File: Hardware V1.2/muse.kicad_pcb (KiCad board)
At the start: 2 copper layers, 71.6 x 61.5 mm, 53 parts, among them P1 3.5mm_line, P2 3.5mm_line, P3 RCA, P4 RCA, P8 ATX_PS_ON, P9 LED_Signal, Q1 FQP30N06L, Q2 FQP30N06L, Q3 FQP30N06L, Q4 FQP30N06L, Q5 FQP30N06L, Q6 FQP30N06L, SW1 PWR_SW, U1 MSGEQ7, U2 MSGEQ7, U3 74LS595, U4 Spark_Core

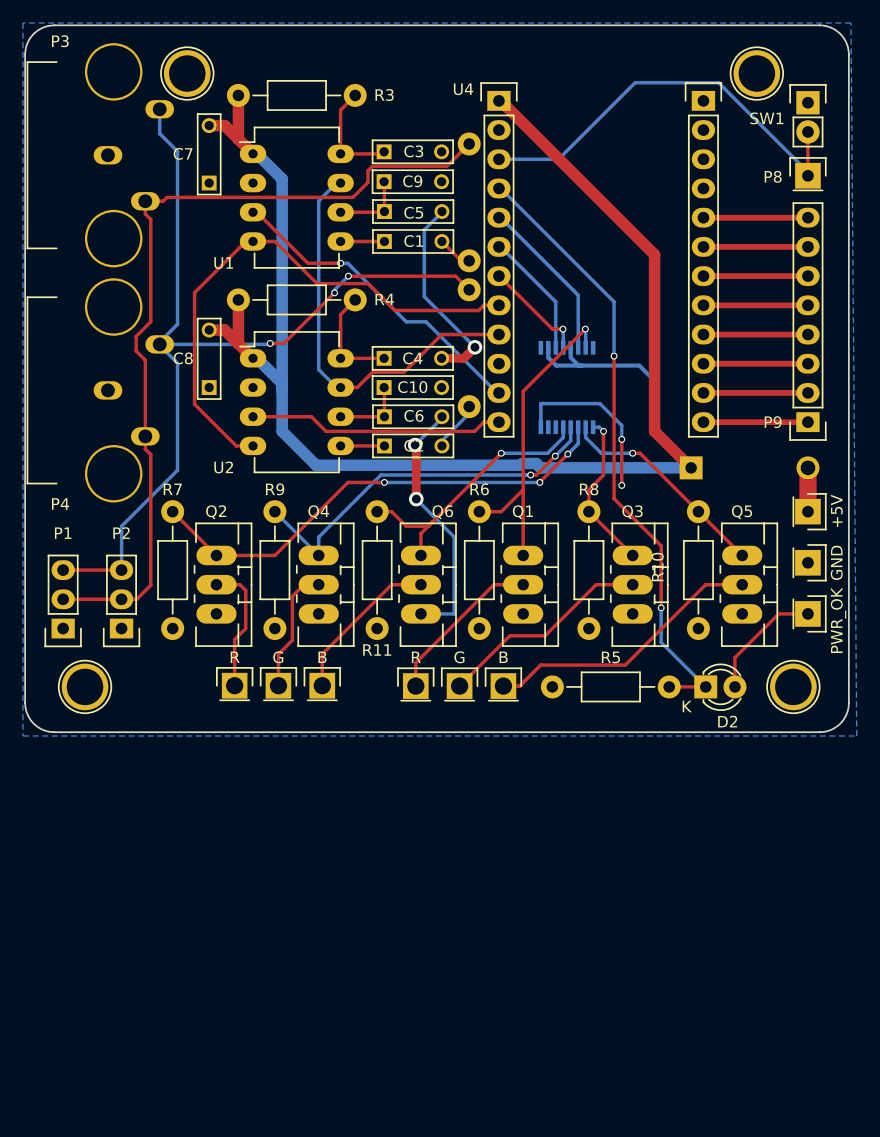
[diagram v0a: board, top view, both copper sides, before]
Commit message: Updated footprints, added gnd fill keep out
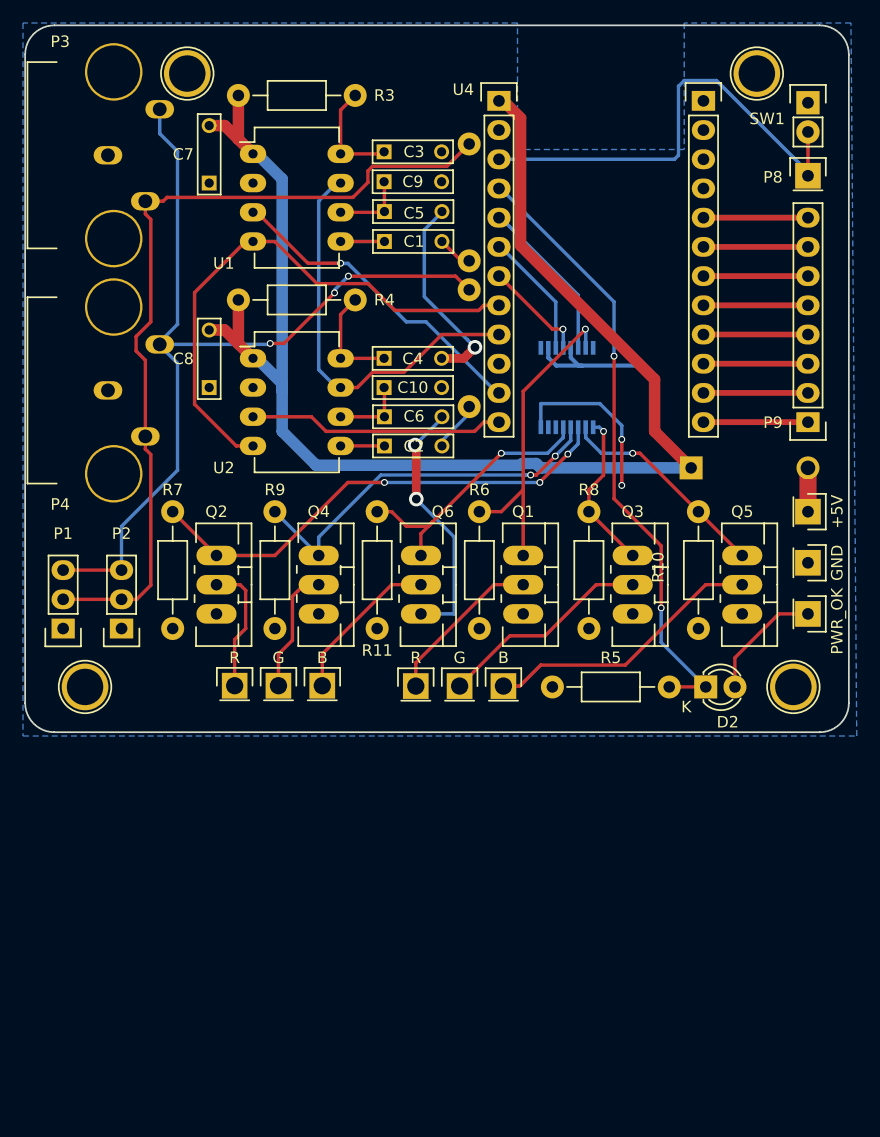
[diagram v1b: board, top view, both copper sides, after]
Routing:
- net /ATX_PWR_ON: track 33.2 -> 36.8 mm
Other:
- board text added: "(1.2)"
- board text removed: "(1.1)"
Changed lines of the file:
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@@
     (thickness 1.6)
     (drawings 11)
-    (tracks 285)
+    (tracks 289)
     (zones 0)
     (modules 53)
@@
     )
   )
-  (gr_text "(1.1)" (at 145.923 94.234 90) (layer B.SilkS)
+  (gr_text "(1.2)" (at 145.923 94.234 90) (layer B.SilkS)
     (effects (font (size 1 1) (thickness 0.2)) (justify left mirror))
   )
@@
   (segment (start 114.935 84.365) (end 114.905 84.335) (width 0.3) (layer F.Cu) (net 8))
   (segment (start 114.935 86.995) (end 111.125 86.995) (width 0.3) (layer F.Cu) (net 8) (status 30))
+  (segment (start 124.894362 77.305728) (end 125.275728 77.305728) (width 1) (layer F.Cu) (net 9))
+  (segment (start 138.43 101.535) (end 138.43 106.045) (width 1) (layer F.Cu) (net 9))
+  (segment (start 125.275728 77.305728) (end 126.775728 78.805728) (width 1) (layer F.Cu) (net 9))
+  (segment (start 126.775728 78.805728) (end 126.775728 89.880728) (width 1) (layer F.Cu) (net 9))
+  (segment (start 126.775728 89.880728) (end 138.43 101.535) (width 1) (layer F.Cu) (net 9))
+  (segment (start 138.43 106.045) (end 141.605 109.22) (width 1) (layer F.Cu) (net 9))
   (segment (start 103.855 99.695) (end 103.505 99.695) (width 1) (layer F.Cu) (net 9) (status 30))
   (segment (start 103.855 81.915) (end 103.505 81.915) (width 1) (layer F.Cu) (net 9) (status 30))
@@
   (segment (start 126.786508 108.989988) (end 108.989988 108.989988) (width 1) (layer B.Cu) (net 9))
   (segment (start 106.045 106.045) (end 106.045 102.5466) (width 1) (layer B.Cu) (net 9))
-  (segment (start 125.046762 77.305728) (end 124.894362 77.305728) (width 1) (layer F.Cu) (net 9) (status 30))
-  (segment (start 138.43 90.688966) (end 125.046762 77.305728) (width 1) (layer F.Cu) (net 9) (status 20))
-  (segment (start 138.43 106.045) (end 138.43 90.688966) (width 1) (layer F.Cu) (net 9))
   (segment (start 138.43 106.045) (end 141.605 109.22) (width 0.35) (layer B.Cu) (net 9) (status 20))
   (segment (start 138.43 101.659691) (end 138.43 106.045) (width 0.35) (layer B.Cu) (net 9))
   (segment (start 137.100309 100.33) (end 138.43 101.659691) (width 0.35) (layer B.Cu) (net 9))
   (segment (start 132.114188 100.33) (end 137.100309 100.33) (width 0.35) (layer B.Cu) (net 9))
-  (segment (start 141.605 109.22) (end 138.43 106.045) (width 1) (layer F.Cu) (net 9) (status 10))
   (segment (start 151.765 113.03) (end 151.765 109.22) (width 1.5) (layer F.Cu) (net 10) (status 30))
   (segment (start 139.7 128.27) (end 142.875 128.27) (width 0.3) (layer F.Cu) (net 11) (status 30))
@@
   (segment (start 134.9 94.778966) (end 134.9 99.5) (width 0.3) (layer B.Cu) (net 43))
   (via (at 134.9 99.5) (size 0.6) (drill 0.4) (layers F.Cu B.Cu) (net 43))
-  (segment (start 124.894362 82.385728) (end 130.085272 82.385728) (width 0.3) (layer B.Cu) (net 44))
-  (segment (start 144.005 75.735) (end 151.765 83.495) (width 0.3) (layer B.Cu) (net 44))
-  (segment (start 130.085272 82.385728) (end 136.736 75.735) (width 0.3) (layer B.Cu) (net 44))
-  (segment (start 136.736 75.735) (end 144.005 75.735) (width 0.3) (layer B.Cu) (net 44))
+  (segment (start 124.894362 82.385728) (end 140.154272 82.385728) (width 0.3) (layer B.Cu) (net 44))
+  (segment (start 140.154272 82.385728) (end 140.505 82.035) (width 0.3) (layer B.Cu) (net 44))
+  (segment (start 140.505 82.035) (end 140.505 76.035) (width 0.3) (layer B.Cu) (net 44))
+  (segment (start 143.805 75.535) (end 151.765 83.495) (width 0.3) (layer B.Cu) (net 44))
   (segment (start 151.765 83.495) (end 151.765 83.82) (width 0.3) (layer B.Cu) (net 44))
+  (segment (start 140.505 76.035) (end 141.005 75.535) (width 0.3) (layer B.Cu) (net 44))
+  (segment (start 141.005 75.535) (end 143.805 75.535) (width 0.3) (layer B.Cu) (net 44))
   (zone (net 6) (net_name GND) (layer B.Cu) (hatch edge 0.508)
     (connect_pads (clearance 0.508))
@@
     (polygon
       (pts
-        (xy 83.505 70.535) (xy 83.505 132.535) (xy 156.005 132.535) (xy 155.505 70.535)
+        (xy 83.505 70.535) (xy 83.505 132.535) (xy 156.005 132.535) (xy 155.505 70.535) (xy 141.005 70.535)
+        (xy 141.005 81.535) (xy 126.505 81.535) (xy 126.505 70.535)
       )
     )

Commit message: Updated power paths and RF keepouts
Currently editing transistor GND path sizes
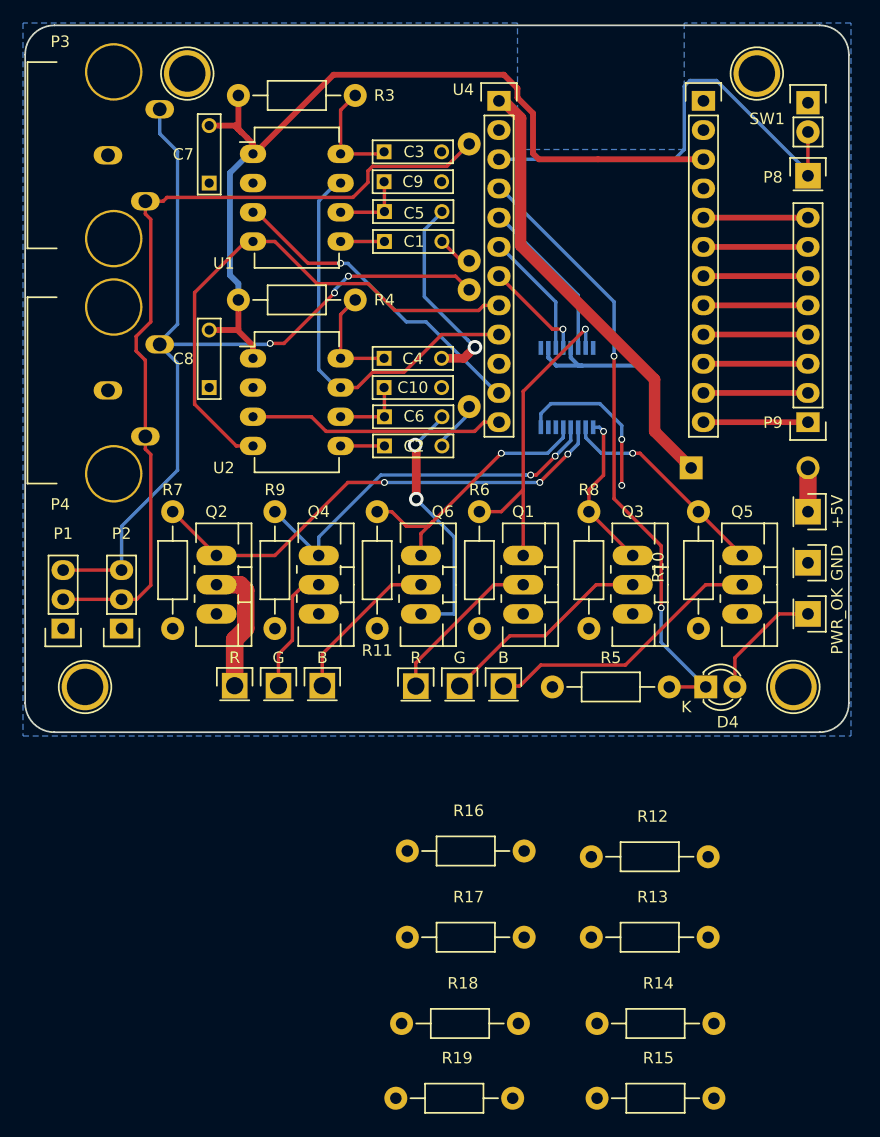
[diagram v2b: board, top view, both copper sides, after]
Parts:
- added R12: 470, Resistors_ThroughHole:Resistor_Horizontal_RM10mm, F.Cu at (138.0, 143.0)
- added R13: 470, Resistors_ThroughHole:Resistor_Horizontal_RM10mm, F.Cu at (138.0, 150.0)
- added R14: 470, Resistors_ThroughHole:Resistor_Horizontal_RM10mm, F.Cu at (138.5, 157.5)
- added R15: 470, Resistors_ThroughHole:Resistor_Horizontal_RM10mm, F.Cu at (138.5, 164.0)
- added R16: 470, Resistors_ThroughHole:Resistor_Horizontal_RM10mm, F.Cu at (122.0, 142.5)
- added R17: 470, Resistors_ThroughHole:Resistor_Horizontal_RM10mm, F.Cu at (122.0, 150.0)
- added R18: 470, Resistors_ThroughHole:Resistor_Horizontal_RM10mm, F.Cu at (121.5, 157.5)
- added R19: 470, Resistors_ThroughHole:Resistor_Horizontal_RM10mm, F.Cu at (121.0, 164.0)
- D1: value 6A -> LED_R
- renumbered D2 to D4
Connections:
- C7 pad 2: +5V -> +3.3V
- C8 pad 2: +5V -> +3.3V
- D1 pad 1: +5V -> Net-(D1-Pad1)
- D1 pad 2: Net-(D1-Pad2) -> +12V
- D4 pad 2: Net-(D2-Pad2) -> Net-(D4-Pad2)
- P9 pad 1: /LED_0 -> Net-(P9-Pad1)
- P9 pad 2: /LED_1 -> Net-(P9-Pad2)
- P9 pad 3: /LED_2 -> Net-(P9-Pad3)
- P9 pad 4: /LED_3 -> Net-(P9-Pad4)
- P9 pad 5: /LED_4 -> Net-(P9-Pad5)
- P9 pad 6: /LED_5 -> Net-(P9-Pad6)
- P9 pad 7: /LED_6 -> Net-(P9-Pad7)
- P9 pad 8: /LED_7 -> Net-(P9-Pad8)
- Q1 pad 2: Net-(D3-Pad1) -> Net-(D1-Pad1)
- Q2 pad 2: Net-(D4-Pad1) -> Net-(D5-Pad1)
- Q3 pad 2: Net-(D5-Pad1) -> Net-(D2-Pad1)
- Q5 pad 2: Net-(D7-Pad1) -> Net-(D3-Pad1)
- Q6 pad 2: Net-(D8-Pad1) -> Net-(D7-Pad1)
- R3 pad 2: +5V -> +3.3V
- R4 pad 2: +5V -> +3.3V
- R5 pad 2: Net-(D2-Pad2) -> Net-(D4-Pad2)
- U1 pad 1: +5V -> +3.3V
- U2 pad 1: +5V -> +3.3V
- U4 pad 22: Net-(U4-Pad22) -> +3.3V
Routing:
- net +5V: track 145.5 -> 52.0 mm
- net +3.3V: track 0.00 -> 79.2 mm
- net Net-(D3-Pad1): track 14.2 -> 32.0 mm
- net Net-(D1-Pad1): track 0.00 -> 11.5 mm
- net Net-(D8-Pad1): track 13.8 -> 2.74 mm
- net Net-(D7-Pad1): track 24.4 -> 15.1 mm
- net Net-(D4-Pad2): track 0.00 -> 5.72 mm
- net Net-(D2-Pad2): track 13.6 -> 7.93 mm
- net Net-(D1-Pad2): track 3.81 -> 0.00 mm
- net +12V: track 0.00 -> 3.81 mm
- net Net-(D2-Pad1): track 0.00 -> 3.18 mm
- net Net-(D4-Pad1): track 11.4 -> 9.38 mm
- net Net-(D5-Pad1): track 18.7 -> 17.6 mm
- net GND: track 55.4 -> 54.9 mm
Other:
- net class 3v3 added: clearance 0.2, trace_width 0.508, via_dia 0.6, via_drill 0.4
